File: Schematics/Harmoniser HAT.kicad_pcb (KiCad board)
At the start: 2 copper layers, 130 x 96 mm, 0 parts

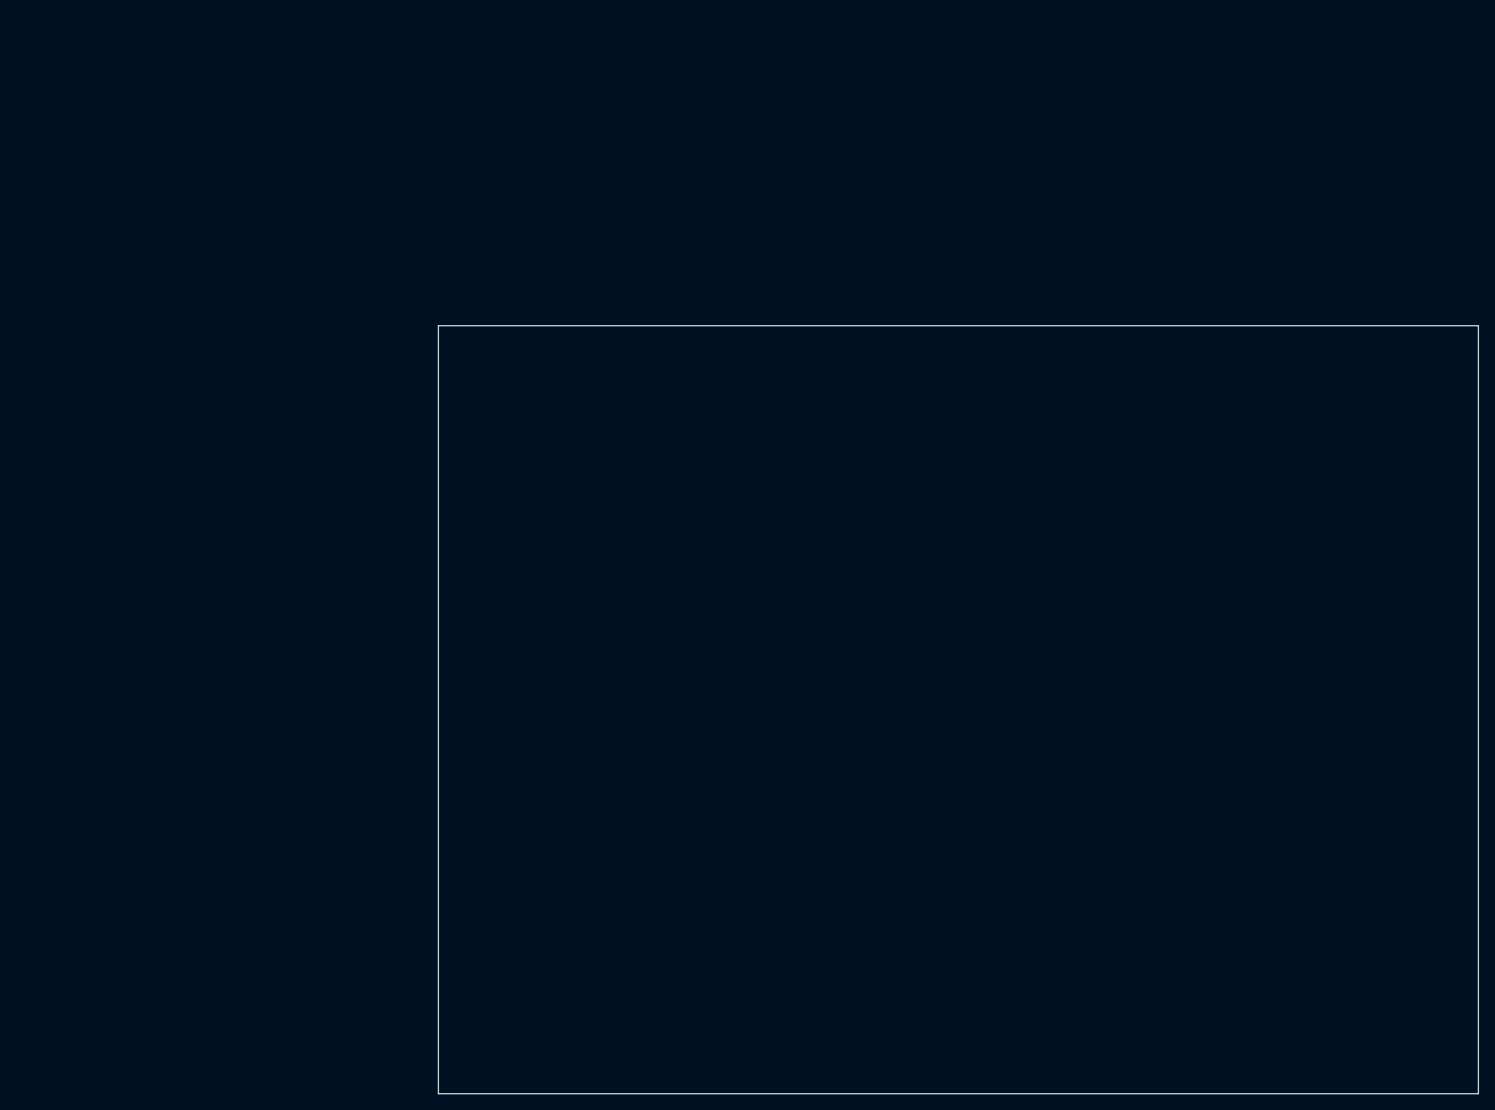
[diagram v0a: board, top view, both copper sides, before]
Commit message: Updated to KiCAD v9
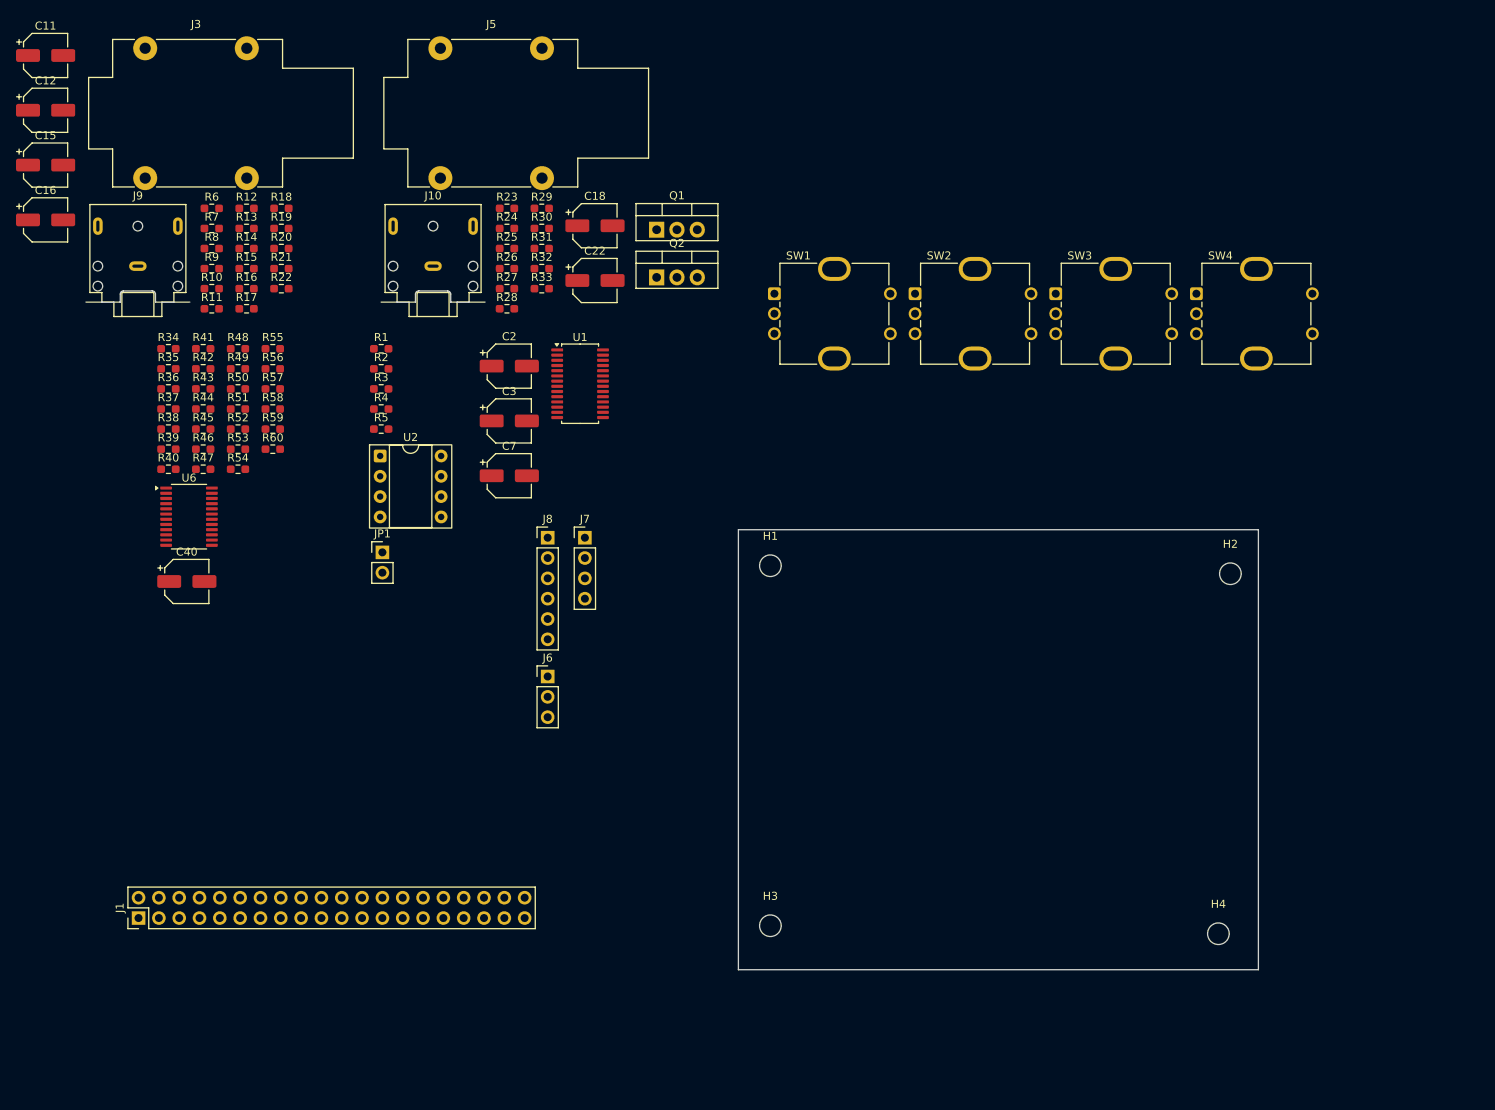
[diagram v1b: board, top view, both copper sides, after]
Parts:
- added C11: 10u, Capacitor_SMD:CP_Elec_5x5.4, F.Cu at (19.9, 18.7)
- added C12: 10u, Capacitor_SMD:CP_Elec_5x5.4, F.Cu at (19.9, 25.6)
- added C15: 10u, Capacitor_SMD:CP_Elec_5x5.4, F.Cu at (19.9, 32.4)
- added C16: 10u, Capacitor_SMD:CP_Elec_5x5.4, F.Cu at (19.9, 39.3)
- added C18: 10u, Capacitor_SMD:CP_Elec_5x5.4, F.Cu at (88.6, 40.0)
- added C2: 10u, Capacitor_SMD:CP_Elec_5x5.4, F.Cu at (77.9, 57.5)
- added C22: 10u, Capacitor_SMD:CP_Elec_5x5.4, F.Cu at (88.6, 46.9)
- added C3: 10u, Capacitor_SMD:CP_Elec_5x5.4, F.Cu at (77.9, 64.4)
- added C40: 10u, Capacitor_SMD:CP_Elec_5x5.4, F.Cu at (37.5, 84.5)
- added C7: 10u, Capacitor_SMD:CP_Elec_5x5.4, F.Cu at (77.9, 71.2)
- added H1: MountingHole, MountingHole:MountingHole_2.7mm_M2.5, F.Cu at (110.5, 82.5)
- added H2: MountingHole, MountingHole:MountingHole_2.7mm_M2.5, F.Cu at (168.0, 83.5)
- added H3: MountingHole, MountingHole:MountingHole_2.7mm_M2.5, F.Cu at (110.5, 127.5)
- added H4: MountingHole, MountingHole:MountingHole_2.7mm_M2.5, F.Cu at (166.5, 128.5)
- added J1: RPi GPIO, Connector_PinHeader_2.54mm:PinHeader_2x20_P2.54mm_Vertical, F.Cu at (31.5, 126.5)
- added J10: Line Out, Connector_Audio:Jack_3.5mm_CUI_SJ1-3523N_Horizontal, F.Cu at (68.3, 45.0)
- added J3: Inst In, Connector_Audio:Jack_6.35mm_Neutrik_NMJ4HHD2_Horizontal, F.Cu at (32.4, 17.8)
- added J5: Inst Out, Connector_Audio:Jack_6.35mm_Neutrik_NMJ4HHD2_Horizontal, F.Cu at (69.2, 17.8)
- added J6: I2C Header, Connector_PinHeader_2.54mm:PinHeader_1x03_P2.54mm_Vertical, F.Cu at (82.7, 96.3)
- added J7: PWR, Connector_PinHeader_2.54mm:PinHeader_1x04_P2.54mm_Vertical, F.Cu at (87.3, 79.0)
- added J8: I2S Header, Connector_PinHeader_2.54mm:PinHeader_1x06_P2.54mm_Vertical, F.Cu at (82.7, 79.0)
- added J9: Line In, Connector_Audio:Jack_3.5mm_CUI_SJ1-3523N_Horizontal, F.Cu at (31.4, 45.0)
- added JP1: Jumper_2_Open, Connector_PinHeader_2.54mm:PinHeader_1x02_P2.54mm_Vertical, F.Cu at (62.0, 80.8)
- added Q1: Q_NPN_BEC, Package_TO_SOT_THT:TO-220-3_Vertical, F.Cu at (96.3, 40.5)
- added Q2: Q_NPN_BEC, Package_TO_SOT_THT:TO-220-3_Vertical, F.Cu at (96.3, 46.5)
- added R1: 3k9, Resistor_SMD:R_0603_1608Metric_Pad0.98x0.95mm_HandSolder, F.Cu at (61.9, 55.4)
- added R10: 1k, Resistor_SMD:R_0603_1608Metric_Pad0.98x0.95mm_HandSolder, F.Cu at (40.7, 47.9)
- added R11: 0, Resistor_SMD:R_0603_1608Metric_Pad0.98x0.95mm_HandSolder, F.Cu at (40.7, 50.4)
- added R12: 0, Resistor_SMD:R_0603_1608Metric_Pad0.98x0.95mm_HandSolder, F.Cu at (45.0, 37.8)
- added R13: 0, Resistor_SMD:R_0603_1608Metric_Pad0.98x0.95mm_HandSolder, F.Cu at (45.0, 40.3)
- added R14: 0, Resistor_SMD:R_0603_1608Metric_Pad0.98x0.95mm_HandSolder, F.Cu at (45.0, 42.9)
- added R15: 47k, Resistor_SMD:R_0603_1608Metric_Pad0.98x0.95mm_HandSolder, F.Cu at (45.0, 45.4)
- added R16: 0, Resistor_SMD:R_0603_1608Metric_Pad0.98x0.95mm_HandSolder, F.Cu at (45.0, 47.9)
- added R17: 0, Resistor_SMD:R_0603_1608Metric_Pad0.98x0.95mm_HandSolder, F.Cu at (45.0, 50.4)
- added R18: 0, Resistor_SMD:R_0603_1608Metric_Pad0.98x0.95mm_HandSolder, F.Cu at (49.4, 37.8)
- added R19: 10k, Resistor_SMD:R_0603_1608Metric_Pad0.98x0.95mm_HandSolder, F.Cu at (49.4, 40.3)
- added R2: 3k9, Resistor_SMD:R_0603_1608Metric_Pad0.98x0.95mm_HandSolder, F.Cu at (61.9, 57.9)
- added R20: 1k, Resistor_SMD:R_0603_1608Metric_Pad0.98x0.95mm_HandSolder, F.Cu at (49.4, 42.9)
- added R21: 0, Resistor_SMD:R_0603_1608Metric_Pad0.98x0.95mm_HandSolder, F.Cu at (49.4, 45.4)
- added R22: 0, Resistor_SMD:R_0603_1608Metric_Pad0.98x0.95mm_HandSolder, F.Cu at (49.4, 47.9)
- added R23: 7.5k, Resistor_SMD:R_0603_1608Metric_Pad0.98x0.95mm_HandSolder, F.Cu at (77.6, 37.8)
- added R24: 0, Resistor_SMD:R_0603_1608Metric_Pad0.98x0.95mm_HandSolder, F.Cu at (77.6, 40.3)
- added R25: 10k, Resistor_SMD:R_0603_1608Metric_Pad0.98x0.95mm_HandSolder, F.Cu at (77.6, 42.9)
- added R26: 750, Resistor_SMD:R_0603_1608Metric_Pad0.98x0.95mm_HandSolder, F.Cu at (77.6, 45.4)
- added R27: 0, Resistor_SMD:R_0603_1608Metric_Pad0.98x0.95mm_HandSolder, F.Cu at (77.6, 47.9)
- added R28: 0, Resistor_SMD:R_0603_1608Metric_Pad0.98x0.95mm_HandSolder, F.Cu at (77.6, 50.4)
- added R29: 7.5k, Resistor_SMD:R_0603_1608Metric_Pad0.98x0.95mm_HandSolder, F.Cu at (81.9, 37.8)
- added R3: 1k, Resistor_SMD:R_0603_1608Metric_Pad0.98x0.95mm_HandSolder, F.Cu at (61.9, 60.4)
- added R30: 0, Resistor_SMD:R_0603_1608Metric_Pad0.98x0.95mm_HandSolder, F.Cu at (81.9, 40.3)
- added R31: 10k, Resistor_SMD:R_0603_1608Metric_Pad0.98x0.95mm_HandSolder, F.Cu at (81.9, 42.9)
- added R32: 750, Resistor_SMD:R_0603_1608Metric_Pad0.98x0.95mm_HandSolder, F.Cu at (81.9, 45.4)
- added R33: 0, Resistor_SMD:R_0603_1608Metric_Pad0.98x0.95mm_HandSolder, F.Cu at (81.9, 47.9)
- added R34: 10k, Resistor_SMD:R_0603_1608Metric_Pad0.98x0.95mm_HandSolder, F.Cu at (35.2, 55.4)
- added R35: 10k, Resistor_SMD:R_0603_1608Metric_Pad0.98x0.95mm_HandSolder, F.Cu at (35.2, 57.9)
- added R36: 10k, Resistor_SMD:R_0603_1608Metric_Pad0.98x0.95mm_HandSolder, F.Cu at (35.2, 60.4)
- added R37: 10k, Resistor_SMD:R_0603_1608Metric_Pad0.98x0.95mm_HandSolder, F.Cu at (35.2, 62.9)
- added R38: 10k, Resistor_SMD:R_0603_1608Metric_Pad0.98x0.95mm_HandSolder, F.Cu at (35.2, 65.4)
- added R39: 10k, Resistor_SMD:R_0603_1608Metric_Pad0.98x0.95mm_HandSolder, F.Cu at (35.2, 67.9)
- added R4: 22k, Resistor_SMD:R_0603_1608Metric_Pad0.98x0.95mm_HandSolder, F.Cu at (61.9, 62.9)
- added R40: 10k, Resistor_SMD:R_0603_1608Metric_Pad0.98x0.95mm_HandSolder, F.Cu at (35.2, 70.4)
- added R41: 10k, Resistor_SMD:R_0603_1608Metric_Pad0.98x0.95mm_HandSolder, F.Cu at (39.6, 55.4)
- added R42: 10k, Resistor_SMD:R_0603_1608Metric_Pad0.98x0.95mm_HandSolder, F.Cu at (39.6, 57.9)
- added R43: 10k, Resistor_SMD:R_0603_1608Metric_Pad0.98x0.95mm_HandSolder, F.Cu at (39.6, 60.4)
- added R44: 10k, Resistor_SMD:R_0603_1608Metric_Pad0.98x0.95mm_HandSolder, F.Cu at (39.6, 62.9)
- added R45: 10k, Resistor_SMD:R_0603_1608Metric_Pad0.98x0.95mm_HandSolder, F.Cu at (39.6, 65.4)
- added R46: 10k, Resistor_SMD:R_0603_1608Metric_Pad0.98x0.95mm_HandSolder, F.Cu at (39.6, 67.9)
- added R47: 10k, Resistor_SMD:R_0603_1608Metric_Pad0.98x0.95mm_HandSolder, F.Cu at (39.6, 70.4)
- added R48: 10k, Resistor_SMD:R_0603_1608Metric_Pad0.98x0.95mm_HandSolder, F.Cu at (44.0, 55.4)
- added R49: 10k, Resistor_SMD:R_0603_1608Metric_Pad0.98x0.95mm_HandSolder, F.Cu at (44.0, 57.9)
- added R5: 10k, Resistor_SMD:R_0603_1608Metric_Pad0.98x0.95mm_HandSolder, F.Cu at (61.9, 65.4)
- added R50: 10k, Resistor_SMD:R_0603_1608Metric_Pad0.98x0.95mm_HandSolder, F.Cu at (44.0, 60.4)
- added R51: 10k, Resistor_SMD:R_0603_1608Metric_Pad0.98x0.95mm_HandSolder, F.Cu at (44.0, 62.9)
- added R52: 10k, Resistor_SMD:R_0603_1608Metric_Pad0.98x0.95mm_HandSolder, F.Cu at (44.0, 65.4)
- added R53: 10k, Resistor_SMD:R_0603_1608Metric_Pad0.98x0.95mm_HandSolder, F.Cu at (44.0, 67.9)
- added R54: 10k, Resistor_SMD:R_0603_1608Metric_Pad0.98x0.95mm_HandSolder, F.Cu at (44.0, 70.4)
- added R55: 10k, Resistor_SMD:R_0603_1608Metric_Pad0.98x0.95mm_HandSolder, F.Cu at (48.3, 55.4)
- added R56: 10k, Resistor_SMD:R_0603_1608Metric_Pad0.98x0.95mm_HandSolder, F.Cu at (48.3, 57.9)
- added R57: 10k, Resistor_SMD:R_0603_1608Metric_Pad0.98x0.95mm_HandSolder, F.Cu at (48.3, 60.4)
- added R58: 10k, Resistor_SMD:R_0603_1608Metric_Pad0.98x0.95mm_HandSolder, F.Cu at (48.3, 62.9)
- added R59: 10k, Resistor_SMD:R_0603_1608Metric_Pad0.98x0.95mm_HandSolder, F.Cu at (48.3, 65.4)
- added R6: 27k, Resistor_SMD:R_0603_1608Metric_Pad0.98x0.95mm_HandSolder, F.Cu at (40.7, 37.8)
- added R60: 10k, Resistor_SMD:R_0603_1608Metric_Pad0.98x0.95mm_HandSolder, F.Cu at (48.3, 67.9)
- added R7: 0, Resistor_SMD:R_0603_1608Metric_Pad0.98x0.95mm_HandSolder, F.Cu at (40.7, 40.3)
- added R8: 0, Resistor_SMD:R_0603_1608Metric_Pad0.98x0.95mm_HandSolder, F.Cu at (40.7, 42.9)
- added R9: 27k, Resistor_SMD:R_0603_1608Metric_Pad0.98x0.95mm_HandSolder, F.Cu at (40.7, 45.4)
- added SW1: RotaryEncoder_Switch, Rotary_Encoder:RotaryEncoder_Bourns_Vertical_PEC12R-3x17F-Sxxxx, F.Cu at (111.0, 48.5)
- added SW2: RotaryEncoder_Switch, Rotary_Encoder:RotaryEncoder_Bourns_Vertical_PEC12R-3x17F-Sxxxx, F.Cu at (128.6, 48.5)
- added SW3: RotaryEncoder_Switch, Rotary_Encoder:RotaryEncoder_Bourns_Vertical_PEC12R-3x17F-Sxxxx, F.Cu at (146.2, 48.5)
- added SW4: RotaryEncoder_Switch, Rotary_Encoder:RotaryEncoder_Bourns_Vertical_PEC12R-3x17F-Sxxxx, F.Cu at (163.8, 48.5)
- added U1: PCM3060, Package_SO:TSSOP-28_4.4x9.7mm_P0.65mm, F.Cu at (86.7, 59.8)
- added U2: 24LC256, Package_DIP:DIP-8_W7.62mm_Socket, F.Cu at (61.7, 68.8)
- added U6: PCA9555PW, Package_SO:TSSOP-24_4.4x7.8mm_P0.65mm, F.Cu at (37.8, 76.4)
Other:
- board size 130 x 96 mm -> 65 x 55 mm
- board text added: "OLED DISPLAY"

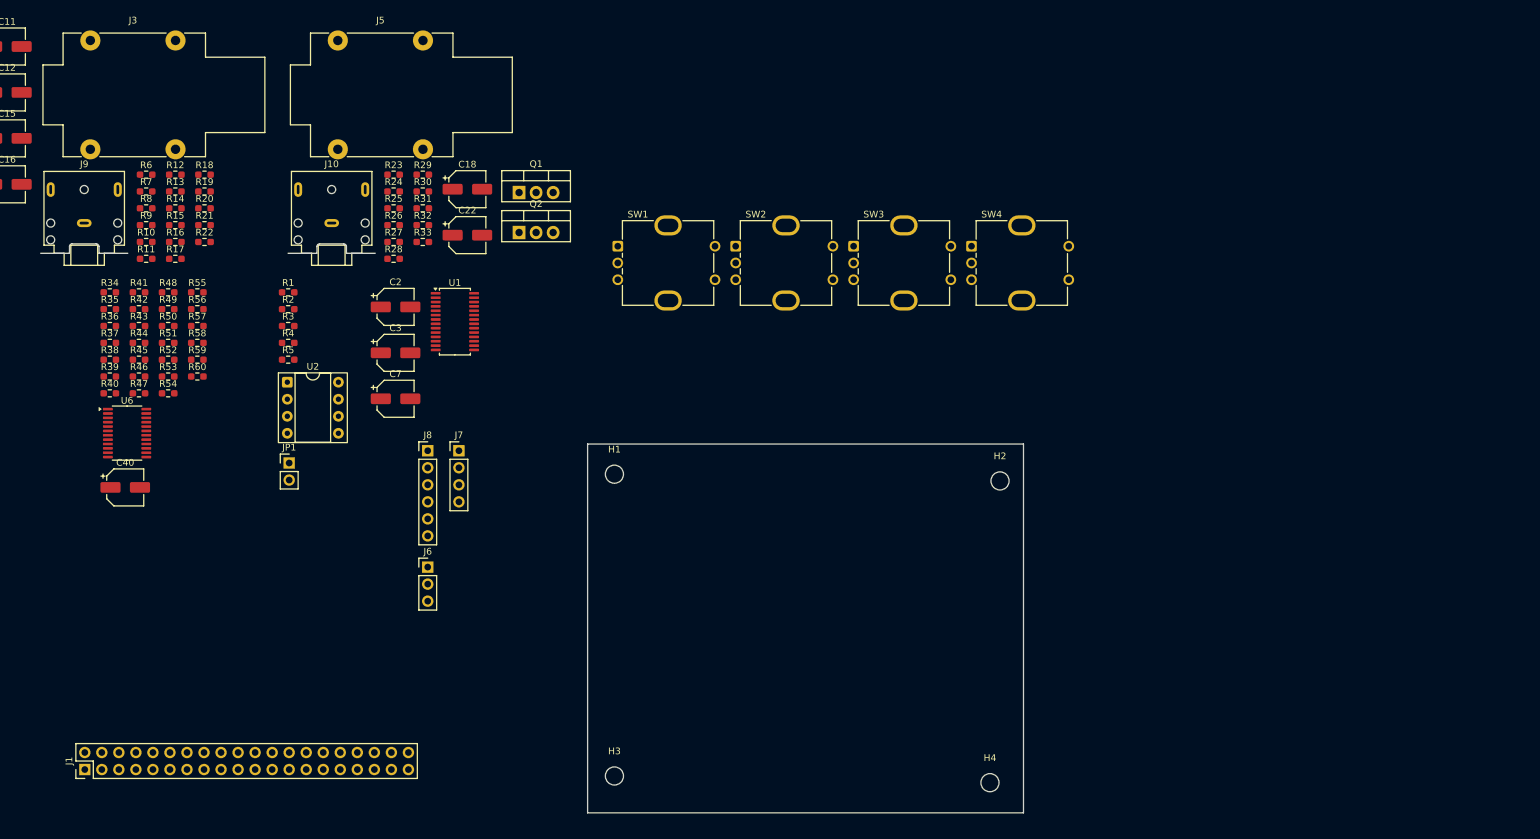
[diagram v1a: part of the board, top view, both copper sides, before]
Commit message: Added all footprints, updated PCB
Added footprints using uni available components where possible. Might be necessary to change op-amps as they are large and not made for audio. PCB has a mockup of component placements but probably needs expanded.
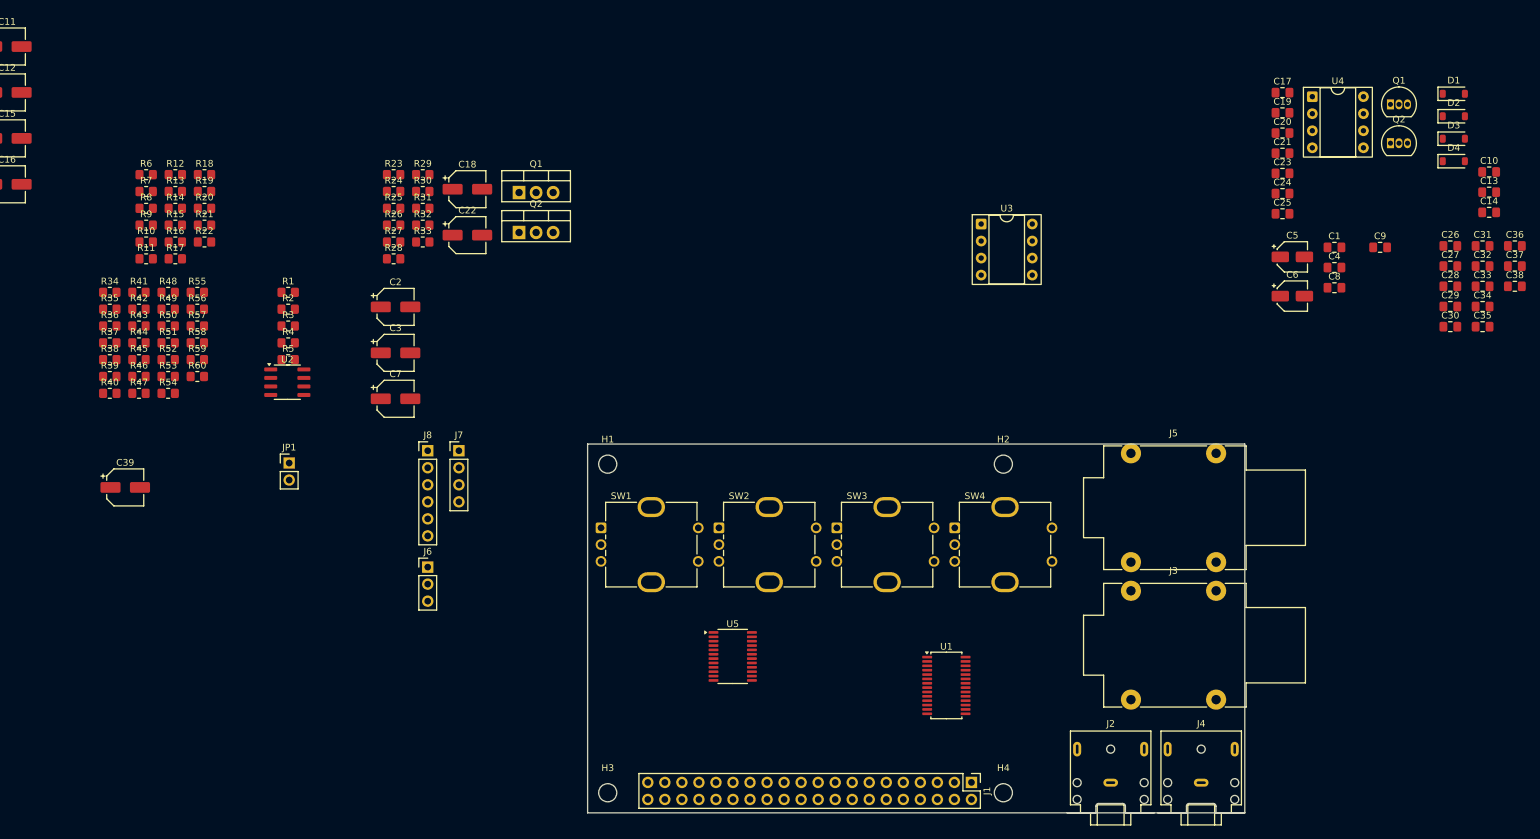
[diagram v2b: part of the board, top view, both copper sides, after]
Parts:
- added C1: 0.1u, Capacitor_SMD:C_0805_2012Metric_Pad1.18x1.45mm_HandSolder, F.Cu at (217.9, 48.7)
- added C10: 330p, Capacitor_SMD:C_0805_2012Metric_Pad1.18x1.45mm_HandSolder, F.Cu at (240.9, 37.4)
- added C13: 0.1u, Capacitor_SMD:C_0805_2012Metric_Pad1.18x1.45mm_HandSolder, F.Cu at (240.9, 40.4)
- added C14: 330p, Capacitor_SMD:C_0805_2012Metric_Pad1.18x1.45mm_HandSolder, F.Cu at (240.9, 43.5)
- added C17: 470p, Capacitor_SMD:C_0805_2012Metric_Pad1.18x1.45mm_HandSolder, F.Cu at (210.1, 25.6)
- added C19: 3.3n, Capacitor_SMD:C_0805_2012Metric_Pad1.18x1.45mm_HandSolder, F.Cu at (210.1, 28.6)
- added C20: 0.1u, Capacitor_SMD:C_0805_2012Metric_Pad1.18x1.45mm_HandSolder, F.Cu at (210.1, 31.6)
- added C21: 470p, Capacitor_SMD:C_0805_2012Metric_Pad1.18x1.45mm_HandSolder, F.Cu at (210.1, 34.6)
- added C23: 3.3n, Capacitor_SMD:C_0805_2012Metric_Pad1.18x1.45mm_HandSolder, F.Cu at (210.1, 37.6)
- added C24: 0.1u, Capacitor_SMD:C_0805_2012Metric_Pad1.18x1.45mm_HandSolder, F.Cu at (210.1, 40.6)
- added C25: 0.1u, Capacitor_SMD:C_0805_2012Metric_Pad1.18x1.45mm_HandSolder, F.Cu at (210.1, 43.7)
- added C26: 0.01u, Capacitor_SMD:C_0805_2012Metric_Pad1.18x1.45mm_HandSolder, F.Cu at (235.2, 48.5)
- added C27: 0.01u, Capacitor_SMD:C_0805_2012Metric_Pad1.18x1.45mm_HandSolder, F.Cu at (235.2, 51.5)
- added C28: 0.01u, Capacitor_SMD:C_0805_2012Metric_Pad1.18x1.45mm_HandSolder, F.Cu at (235.2, 54.5)
- added C29: 0.01u, Capacitor_SMD:C_0805_2012Metric_Pad1.18x1.45mm_HandSolder, F.Cu at (235.2, 57.5)
- added C30: 0.01u, Capacitor_SMD:C_0805_2012Metric_Pad1.18x1.45mm_HandSolder, F.Cu at (235.2, 60.5)
- added C31: 0.01u, Capacitor_SMD:C_0805_2012Metric_Pad1.18x1.45mm_HandSolder, F.Cu at (240.0, 48.5)
- added C32: 0.01u, Capacitor_SMD:C_0805_2012Metric_Pad1.18x1.45mm_HandSolder, F.Cu at (240.0, 51.5)
- added C33: 0.01u, Capacitor_SMD:C_0805_2012Metric_Pad1.18x1.45mm_HandSolder, F.Cu at (240.0, 54.5)
- added C34: 0.01u, Capacitor_SMD:C_0805_2012Metric_Pad1.18x1.45mm_HandSolder, F.Cu at (240.0, 57.5)
- added C35: 0.01u, Capacitor_SMD:C_0805_2012Metric_Pad1.18x1.45mm_HandSolder, F.Cu at (240.0, 60.5)
- added C36: 0.01u, Capacitor_SMD:C_0805_2012Metric_Pad1.18x1.45mm_HandSolder, F.Cu at (244.8, 48.5)
- added C37: 0.01u, Capacitor_SMD:C_0805_2012Metric_Pad1.18x1.45mm_HandSolder, F.Cu at (244.8, 51.5)
- added C38: 0.1u, Capacitor_SMD:C_0805_2012Metric_Pad1.18x1.45mm_HandSolder, F.Cu at (244.8, 54.5)
- added C4: 0.1u, Capacitor_SMD:C_0805_2012Metric_Pad1.18x1.45mm_HandSolder, F.Cu at (217.9, 51.7)
- added C5: 4.7u, Capacitor_SMD:CP_Elec_4x5.7, F.Cu at (211.6, 50.1)
- added C6: 4.7u, Capacitor_SMD:CP_Elec_4x5.7, F.Cu at (211.6, 55.9)
- added C8: 0.1u, Capacitor_SMD:C_0805_2012Metric_Pad1.18x1.45mm_HandSolder, F.Cu at (217.9, 54.7)
- added C9: 0.1u, Capacitor_SMD:C_0805_2012Metric_Pad1.18x1.45mm_HandSolder, F.Cu at (224.7, 48.7)
- added D1: 1N4148W, Diode_SMD:D_SOD-123, F.Cu at (235.7, 25.8)
- added D2: 1N4148W, Diode_SMD:D_SOD-123, F.Cu at (235.7, 29.1)
- added D3: 1N4148W, Diode_SMD:D_SOD-123, F.Cu at (235.7, 32.5)
- added D4: 1N4148W, Diode_SMD:D_SOD-123, F.Cu at (235.7, 35.8)
- added Q1: BC547, Package_TO_SOT_THT:TO-92_Inline, F.Cu at (226.2, 27.4)
- added Q2: BC547, Package_TO_SOT_THT:TO-92_Inline, F.Cu at (226.2, 33.1)
- added U3: Opamp_Dual, Package_DIP:DIP-8_W7.62mm_Socket, F.Cu at (165.2, 45.2)
- added U4: Opamp_Dual, Package_DIP:DIP-8_W7.62mm_Socket, F.Cu at (214.6, 26.2)
- R1, R10, R11, R12, R13, R14, R15, R16, R17, R18, R19, R2, R20, R21, R22, R23, R24, R25, R26, R27, R28, R29, R3, R30, R31, R32, R33, R34, R35, R36, R37, R38, R39, R4, R40, R41, R42, R43, R44, R45, R46, R47, R48, R49, R5, R50, R51, R52, R53, R54, R55, R56, R57, R58, R59, R6, R60, R7, R8, R9: footprint Resistor_SMD:R_0603_1608Metric_Pad0.98x0.95mm_HandSolder -> Resistor_SMD:R_0805_2012Metric_Pad1.20x1.40mm_HandSolder
- U2: footprint Package_DIP:DIP-8_W7.62mm_Socket -> Package_SO:SOIC-8_3.9x4.9mm_P1.27mm
- moved J3 175.5 mm to (187.5, 99.9)
- moved J2 174.3 mm to (184.5, 128.5)
- moved J4 154.2 mm to (198.0, 128.5)
- moved J5 133.3 mm to (187.5, 79.4)
- moved J1 132.2 mm to (163.7, 128.5), turned to -90 degrees
- moved U5 96.3 mm to (128.1, 109.7)
- moved U1 91.2 mm to (160.0, 114.0)
- moved SW1 42.1 mm to (108.5, 90.5)
- moved SW2 42.1 mm to (126.1, 90.5)
- moved SW3 42.1 mm to (143.7, 90.5)
- moved SW4 42.1 mm to (161.2, 90.5)
- moved H3 2.69 mm to (109.5, 130.0)
- moved H2 2.55 mm to (168.5, 81.0)
- moved H4 2.50 mm to (168.5, 130.0)
- moved H1 1.80 mm to (109.5, 81.0)
- renumbered C40 to C39, J9 to J2, J10 to J4, U6 to U5
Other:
- board size 65 x 55 mm -> 98 x 55 mm
- board text added: "Spacings not exact (yet)"
